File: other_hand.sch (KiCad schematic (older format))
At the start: 49 parts

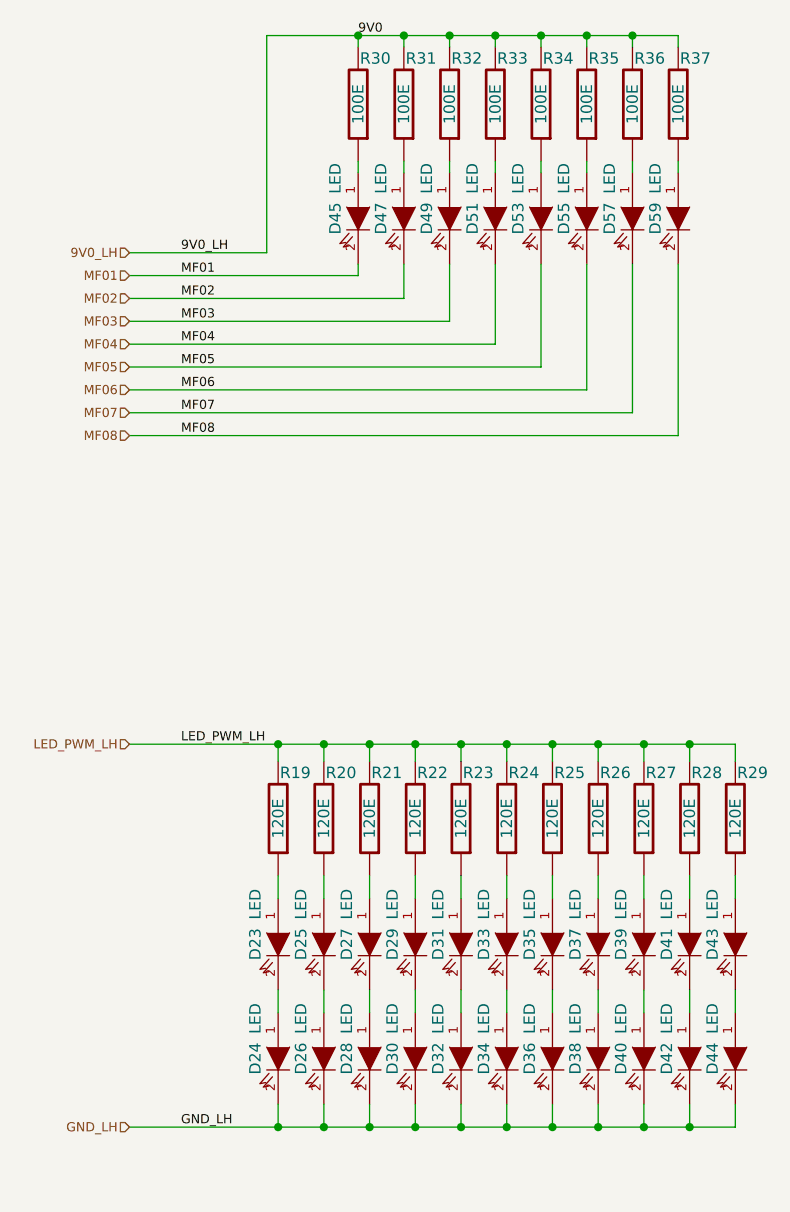
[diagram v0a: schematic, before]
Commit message: WiP - decided to add a IR Transmitter in the spare available board space.
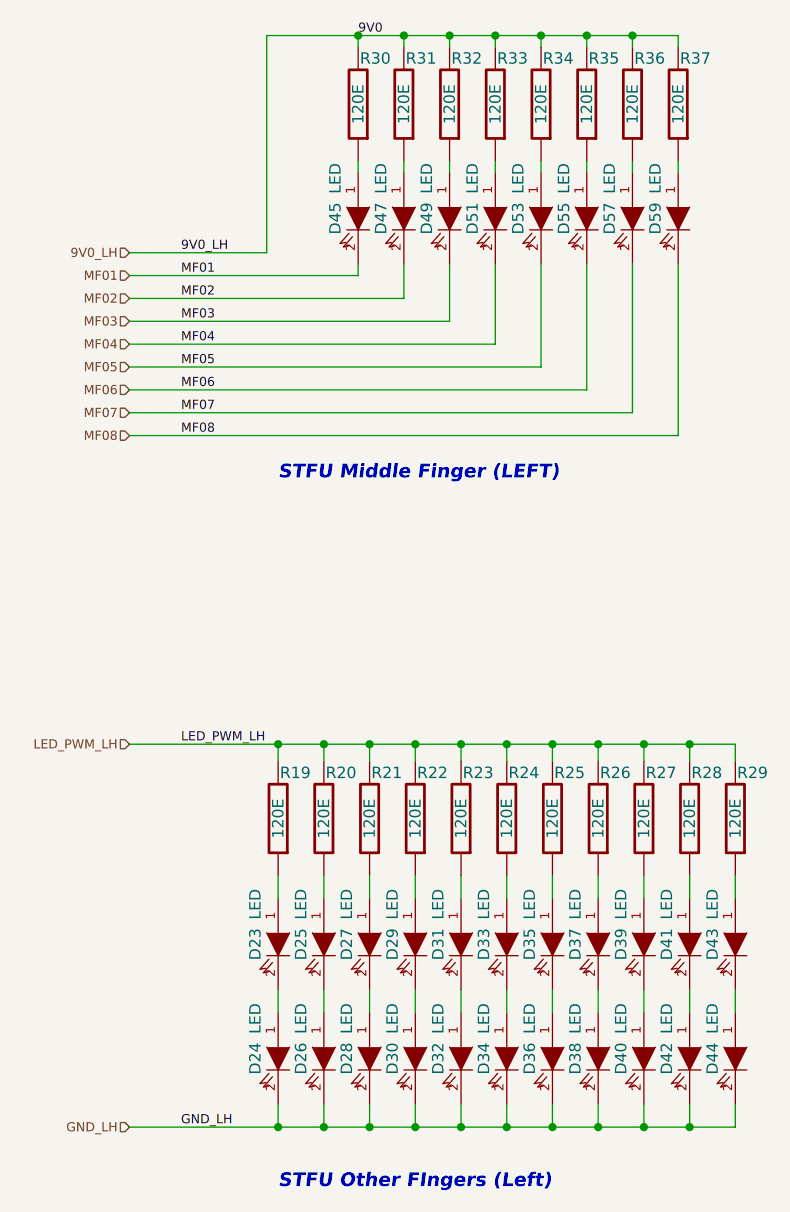
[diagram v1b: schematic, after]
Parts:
- D23, D24, D25, D26, D27, D28, D29, D30, D31, D32, D33, D34, D35, D36, D37, D38, D39, D40, D41, D42, D43, D44, D45, D47, D49, D51, D53, D55, D57, D59: footprint (none) -> d_1206
- R30, R31, R32, R33, R34, R35, R36, R37: value 100E -> 120E
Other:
- note added: "STFU Middle Finger (LEFT)"
- note added: "STFU Other FIngers (Left)"
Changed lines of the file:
@@
-EESchema Schematic File Version 2  date 7/17/2012 5:33:20 PM
+EESchema Schematic File Version 2  date 7/18/2012 6:00:20 PM
 LIBS:stfu
 LIBS:power
@@
 $Descr A4 11700 8267
 encoding utf-8
-Sheet 2 2
+Sheet 2 3
 Title ""
-Date "17 jul 2012"
+Date "18 jul 2012"
 Rev ""
 Comp ""
@@
 Comment4 ""
 $EndDescr
+Text Notes 6800 6700 0    60   Italic 12
+STFU Other FIngers (Left)
+Text Notes 6800 3600 0    60   Italic 12
+STFU Middle Finger (LEFT)
 Text HLabel 6150 2600 0    40   Input ~ 0
 9V0_LH
@@
 F 0 "D23" H 6800 5525 50  0000 C CNN
 F 1 "LED" H 6625 5525 50  0000 C CNN
+F 2 "d_1206" H 6625 5625 50  0001 C CNN
 	1    6800 5625
 	0    1    1    0
@@
 F 0 "D24" H 6800 6025 50  0000 C CNN
 F 1 "LED" H 6625 6025 50  0000 C CNN
+F 2 "d_1206" H 6625 6125 50  0001 C CNN
 	1    6800 6125
 	0    1    1    0
@@
 F 0 "D43" H 8800 5525 50  0000 C CNN
 F 1 "LED" H 8625 5525 50  0000 C CNN
+F 2 "d_1206" H 8625 5625 50  0001 C CNN
 	1    8800 5625
 	0    1    1    0
@@
 F 0 "D44" H 8800 6025 50  0000 C CNN
 F 1 "LED" H 8625 6025 50  0000 C CNN
+F 2 "d_1206" H 8625 6125 50  0001 C CNN
 	1    8800 6125
 	0    1    1    0
@@
 F 0 "D41" H 8600 5525 50  0000 C CNN
 F 1 "LED" H 8425 5525 50  0000 C CNN
+F 2 "d_1206" H 8425 5625 50  0001 C CNN
 	1    8600 5625
 	0    1    1    0
@@
 F 0 "D42" H 8600 6025 50  0000 C CNN
 F 1 "LED" H 8425 6025 50  0000 C CNN
+F 2 "d_1206" H 8425 6125 50  0001 C CNN
 	1    8600 6125
 	0    1    1    0
@@
 F 0 "D40" H 8400 6025 50  0000 C CNN
 F 1 "LED" H 8225 6025 50  0000 C CNN
+F 2 "d_1206" H 8225 6125 50  0001 C CNN
 	1    8400 6125
 	0    1    1    0
@@
 F 0 "D39" H 8400 5525 50  0000 C CNN
 F 1 "LED" H 8225 5525 50  0000 C CNN
+F 2 "d_1206" H 8225 5625 50  0001 C CNN
 	1    8400 5625
 	0    1    1    0
@@
 F 0 "D31" H 7600 5525 50  0000 C CNN
 F 1 "LED" H 7425 5525 50  0000 C CNN
+F 2 "d_1206" H 7425 5625 50  0001 C CNN
 	1    7600 5625
 	0    1    1    0
@@
 F 0 "D32" H 7600 6025 50  0000 C CNN
 F 1 "LED" H 7425 6025 50  0000 C CNN
+F 2 "d_1206" H 7425 6125 50  0001 C CNN
 	1    7600 6125
 	0    1    1    0
@@
 F 0 "D34" H 7800 6025 50  0000 C CNN
 F 1 "LED" H 7625 6025 50  0000 C CNN
+F 2 "d_1206" H 7625 6125 50  0001 C CNN
 	1    7800 6125
 	0    1    1    0
@@
 F 0 "D33" H 7800 5525 50  0000 C CNN
 F 1 "LED" H 7625 5525 50  0000 C CNN
+F 2 "d_1206" H 7625 5625 50  0001 C CNN
 	1    7800 5625
 	0    1    1    0
@@
 F 0 "D37" H 8200 5525 50  0000 C CNN
 F 1 "LED" H 8025 5525 50  0000 C CNN
+F 2 "d_1206" H 8025 5625 50  0001 C CNN
 	1    8200 5625
 	0    1    1    0
@@
 F 0 "D38" H 8200 6025 50  0000 C CNN
 F 1 "LED" H 8025 6025 50  0000 C CNN
+F 2 "d_1206" H 8025 6125 50  0001 C CNN
 	1    8200 6125
 	0    1    1    0
@@
 F 0 "D36" H 8000 6025 50  0000 C CNN
 F 1 "LED" H 7825 6025 50  0000 C CNN
+F 2 "d_1206" H 7825 6125 50  0001 C CNN
 	1    8000 6125
 	0    1    1    0
@@
 F 0 "D35" H 8000 5525 50  0000 C CNN
 F 1 "LED" H 7825 5525 50  0000 C CNN
+F 2 "d_1206" H 7825 5625 50  0001 C CNN
 	1    8000 5625
 	0    1    1    0
@@
 F 0 "D27" H 7200 5525 50  0000 C CNN
 F 1 "LED" H 7025 5525 50  0000 C CNN
+F 2 "d_1206" H 7025 5625 50  0001 C CNN
 	1    7200 5625
 	0    1    1    0
@@
 F 0 "D28" H 7200 6025 50  0000 C CNN
 F 1 "LED" H 7025 6025 50  0000 C CNN
+F 2 "d_1206" H 7025 6125 50  0001 C CNN
 	1    7200 6125
 	0    1    1    0
@@
 F 0 "D30" H 7400 6025 50  0000 C CNN
 F 1 "LED" H 7225 6025 50  0000 C CNN
+F 2 "d_1206" H 7225 6125 50  0001 C CNN
 	1    7400 6125
 	0    1    1    0
@@
 F 0 "D29" H 7400 5525 50  0000 C CNN
 F 1 "LED" H 7225 5525 50  0000 C CNN
+F 2 "d_1206" H 7225 5625 50  0001 C CNN
 	1    7400 5625
 	0    1    1    0
@@
 F 0 "D25" H 7000 5525 50  0000 C CNN
 F 1 "LED" H 6825 5525 50  0000 C CNN
+F 2 "d_1206" H 6825 5625 50  0001 C CNN
 	1    7000 5625
 	0    1    1    0
@@
 F 0 "D26" H 7000 6025 50  0000 C CNN
 F 1 "LED" H 6825 6025 50  0000 C CNN
+F 2 "d_1206" H 6825 6125 50  0001 C CNN
 	1    7000 6125
 	0    1    1    0
@@
 F 0 "D45" H 7150 2350 50  0000 C CNN
 F 1 "LED" H 6975 2350 50  0000 C CNN
+F 2 "d_1206" H 6975 2450 50  0001 C CNN
 	1    7150 2450
 	0    1    1    0
@@
 F 0 "D47" H 7350 2350 50  0000 C CNN
 F 1 "LED" H 7175 2350 50  0000 C CNN
+F 2 "d_1206" H 7175 2450 50  0001 C CNN
 	1    7350 2450
 	0    1    1    0
@@
 F 0 "D49" H 7550 2350 50  0000 C CNN
 F 1 "LED" H 7375 2350 50  0000 C CNN
+F 2 "d_1206" H 7375 2450 50  0001 C CNN
 	1    7550 2450
 	0    1    1    0
@@
 F 0 "D51" H 7750 2350 50  0000 C CNN
 F 1 "LED" H 7575 2350 50  0000 C CNN
+F 2 "d_1206" H 7575 2450 50  0001 C CNN
 	1    7750 2450
 	0    1    1    0
@@
 F 0 "D53" H 7950 2350 50  0000 C CNN
 F 1 "LED" H 7775 2350 50  0000 C CNN
+F 2 "d_1206" H 7775 2450 50  0001 C CNN
 	1    7950 2450
 	0    1    1    0
@@
 F 0 "D55" H 8150 2350 50  0000 C CNN
 F 1 "LED" H 7975 2350 50  0000 C CNN
+F 2 "d_1206" H 7975 2450 50  0001 C CNN
 	1    8150 2450
 	0    1    1    0
@@
 F 0 "D57" H 8350 2350 50  0000 C CNN
 F 1 "LED" H 8175 2350 50  0000 C CNN
+F 2 "d_1206" H 8175 2450 50  0001 C CNN
 	1    8350 2450
 	0    1    1    0
@@
 F 0 "D59" H 8550 2350 50  0000 C CNN
 F 1 "LED" H 8375 2350 50  0000 C CNN
+F 2 "d_1206" H 8375 2450 50  0001 C CNN
 	1    8550 2450
 	0    1    1    0
@@
 P 7150 1950
 F 0 "R30" H 7075 1750 50  0000 C CNN
-F 1 "100E" V 7150 1950 50  0000 C CNN
+F 1 "120E" V 7150 1950 50  0000 C CNN
 F 2 "r_0805" H 7150 1950 60  0001 C CNN
 	1    7150 1950
@@
 P 7350 1950
 F 0 "R31" H 7275 1750 50  0000 C CNN
-F 1 "100E" V 7350 1950 50  0000 C CNN
+F 1 "120E" V 7350 1950 50  0000 C CNN
 F 2 "r_0805" H 7350 1950 60  0001 C CNN
 	1    7350 1950
@@
 P 7550 1950
 F 0 "R32" H 7475 1750 50  0000 C CNN
-F 1 "100E" V 7550 1950 50  0000 C CNN
+F 1 "120E" V 7550 1950 50  0000 C CNN
 F 2 "r_0805" H 7550 1950 60  0001 C CNN
 	1    7550 1950
@@
 P 7750 1950
 F 0 "R33" H 7675 1750 50  0000 C CNN
-F 1 "100E" V 7750 1950 50  0000 C CNN
+F 1 "120E" V 7750 1950 50  0000 C CNN
 F 2 "r_0805" H 7750 1950 60  0001 C CNN
 	1    7750 1950
@@
 P 7950 1950
 F 0 "R34" H 7875 1750 50  0000 C CNN
-F 1 "100E" V 7950 1950 50  0000 C CNN
+F 1 "120E" V 7950 1950 50  0000 C CNN
 F 2 "r_0805" H 7950 1950 60  0001 C CNN
 	1    7950 1950
@@
 P 8150 1950
 F 0 "R35" H 8075 1750 50  0000 C CNN
-F 1 "100E" V 8150 1950 50  0000 C CNN
+F 1 "120E" V 8150 1950 50  0000 C CNN
 F 2 "r_0805" H 8150 1950 60  0001 C CNN
 	1    8150 1950
@@
 P 8350 1950
 F 0 "R36" H 8275 1750 50  0000 C CNN
-F 1 "100E" V 8350 1950 50  0000 C CNN
+F 1 "120E" V 8350 1950 50  0000 C CNN
 F 2 "r_0805" H 8350 1950 60  0001 C CNN
 	1    8350 1950
@@
 P 8550 1950
 F 0 "R37" H 8475 1750 50  0000 C CNN
-F 1 "100E" V 8550 1950 50  0000 C CNN
+F 1 "120E" V 8550 1950 50  0000 C CNN
 F 2 "r_0805" H 8550 1950 60  0001 C CNN
 	1    8550 1950
